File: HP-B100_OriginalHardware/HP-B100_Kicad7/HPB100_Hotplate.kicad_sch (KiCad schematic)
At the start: 62 parts, among them J1 01x03_RM3.96mm, J2 01x02_JST_RM2.54mm, J3 Conn_01x03, J4 01x04_RM8.25mm, J5 Screw_Terminal_01x02, J6 Conn_01x09, J7 Conn_01x06, J8 Conn_01x10, Q1 BTA16-800B, SW1 SW_Push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

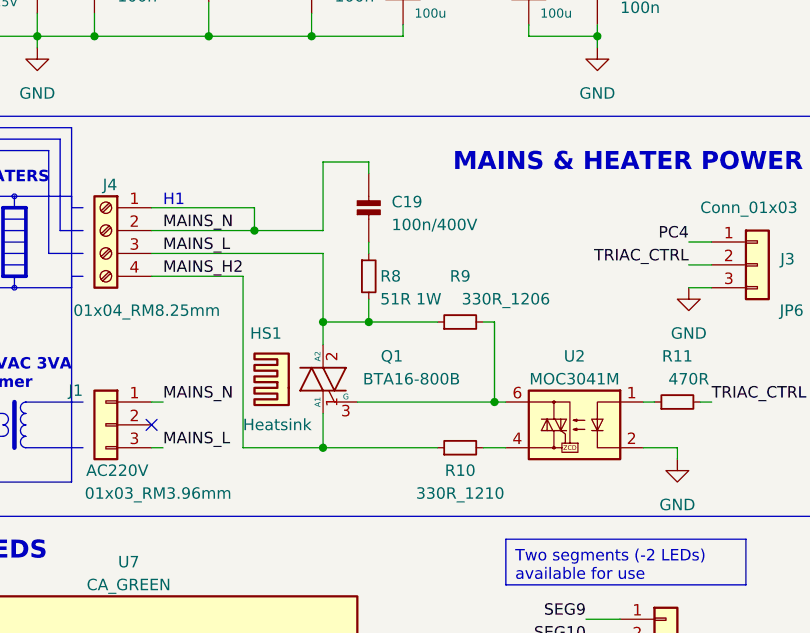
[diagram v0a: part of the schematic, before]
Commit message: fixed snubber circuit
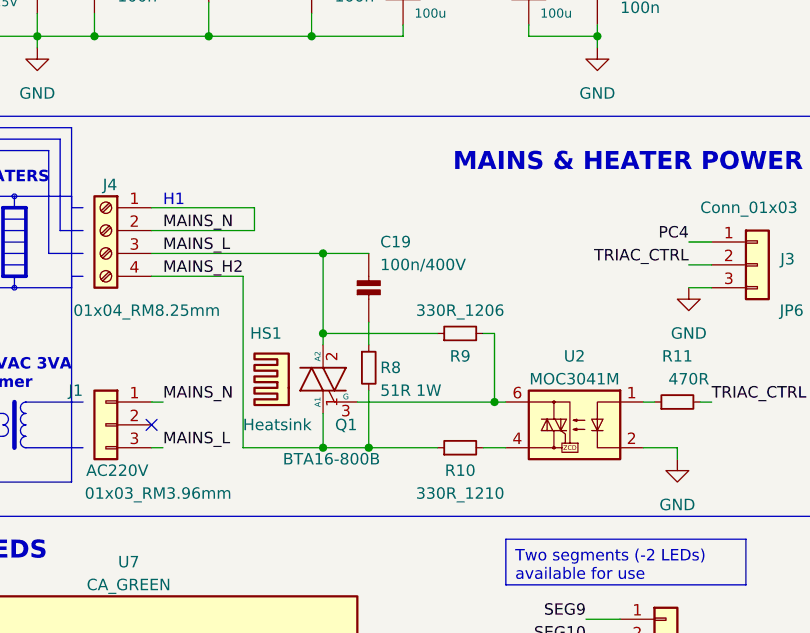
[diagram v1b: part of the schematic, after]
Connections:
- net MAINS_H2: now also R8.2
- net MAINS_L: now also C19.1; no longer R8.2
- net MAINS_N: no longer C19.1
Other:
- moved on the sheet: C19, R8, R9
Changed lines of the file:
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@@
   (junction (at 46.99 167.64) (diameter 0) (color 0 0 0 0)
   )
-  (junction (at 77.47 73.66) (diameter 0) (color 0 0 0 0)
+  (junction (at 77.47 74.93) (diameter 0) (color 0 0 0 0)
   )
   (junction (at 241.3 134.62) (diameter 0) (color 0 0 0 0)
   )
+  (junction (at 82.55 87.63) (diameter 0) (color 0 0 0 0)
+  )
   (junction (at 160.02 147.32) (diameter 0) (color 0 0 0 0)
   )
@@
   (junction (at 142.24 175.26) (diameter 0) (color 0 0 0 0)
   )
-  (junction (at 82.55 73.66) (diameter 0) (color 0 0 0 0)
-  )
   (junction (at 86.36 30.48) (diameter 0) (color 0 0 0 0)
   )
@@
   (junction (at 208.28 116.84) (diameter 0) (color 0 0 0 0)
   )
-  (junction (at 69.85 63.5) (diameter 0) (color 0 0 0 0)
-  )
   (junction (at 196.85 116.84) (diameter 0) (color 0 0 0 0)
   )
@@
   (junction (at 45.72 30.48) (diameter 0) (color 0 0 0 0)
   )
+  (junction (at 77.47 66.04) (diameter 0) (color 0 0 0 0)
+  )
   (junction (at 260.35 125.73) (diameter 0) (color 0 0 0 0)
   )
@@
     (stroke (width 0) (type default))
   )
+  (wire (pts (xy 82.55 87.63) (xy 90.17 87.63))
+    (stroke (width 0) (type default))
+  )
   (wire (pts (xy 24.13 140.97) (xy 29.21 140.97))
     (stroke (width 0) (type default))
@@
     (stroke (width 0) (type default))
   )
+  (wire (pts (xy 77.47 74.93) (xy 77.47 76.2))
+    (stroke (width 0) (type default))
+  )
   (wire (pts (xy 68.58 68.58) (xy 68.58 87.63))
     (stroke (width 0) (type default))
@@
     (stroke (width 0) (type default))
   )
-  (wire (pts (xy 82.55 64.77) (xy 82.55 66.04))
+  (wire (pts (xy 82.55 73.66) (xy 82.55 76.2))
     (stroke (width 0) (type default))
   )
@@
     (stroke (width 0) (type default))
   )
-  (wire (pts (xy 82.55 71.12) (xy 82.55 73.66))
-    (stroke (width 0) (type default))
-  )
   (wire (pts (xy 45.72 30.48) (xy 52.07 30.48))
     (stroke (width 0) (type default))
@@
     (stroke (width 0) (type default))
   )
-  (wire (pts (xy 77.47 66.04) (xy 77.47 73.66))
-    (stroke (width 0) (type default))
-  )
   (polyline (pts (xy 38.1 66.04) (xy 40.64 66.04))
     (stroke (width 0) (type default))
@@
     (stroke (width 0) (type default))
   )
-  (wire (pts (xy 82.55 73.66) (xy 77.47 73.66))
+  (wire (pts (xy 77.47 74.93) (xy 90.17 74.93))
     (stroke (width 0) (type default))
   )
@@
     (stroke (width 0) (type default))
   )
-  (wire (pts (xy 82.55 55.88) (xy 82.55 57.15))
-    (stroke (width 0) (type default))
-  )
   (wire (pts (xy 266.7 22.86) (xy 269.24 22.86))
     (stroke (width 0) (type default))
@@
     (stroke (width 0) (type default))
   )
-  (wire (pts (xy 77.47 63.5) (xy 77.47 55.88))
-    (stroke (width 0) (type default))
-  )
   (wire (pts (xy 72.39 30.48) (xy 76.2 30.48))
     (stroke (width 0) (type default))
@@
     (stroke (width 0) (type default))
   )
-  (wire (pts (xy 69.85 63.5) (xy 77.47 63.5))
-    (stroke (width 0) (type default))
-  )
   (wire (pts (xy 76.2 30.48) (xy 86.36 30.48))
     (stroke (width 0) (type default))
@@
     (stroke (width 0) (type default))
   )
-  (wire (pts (xy 82.55 73.66) (xy 90.17 73.66))
-    (stroke (width 0) (type default))
-  )
   (wire (pts (xy 154.94 134.62) (xy 160.02 134.62))
     (stroke (width 0) (type default))
@@
     (stroke (width 0) (type default))
   )
-  (wire (pts (xy 96.52 73.66) (xy 95.25 73.66))
+  (wire (pts (xy 96.52 74.93) (xy 95.25 74.93))
     (stroke (width 0) (type default))
   )
@@
     (stroke (width 0) (type default))
   )
-  (wire (pts (xy 77.47 87.63) (xy 90.17 87.63))
+  (wire (pts (xy 77.47 87.63) (xy 82.55 87.63))
     (stroke (width 0) (type default))
   )
@@
     (stroke (width 0) (type default))
   )
-  (wire (pts (xy 77.47 55.88) (xy 82.55 55.88))
-    (stroke (width 0) (type default))
-  )
   (wire (pts (xy 106.68 109.22) (xy 110.49 109.22))
     (stroke (width 0) (type default))
@@
     (stroke (width 0) (type default))
   )
+  (wire (pts (xy 82.55 81.28) (xy 82.55 87.63))
+    (stroke (width 0) (type default))
+  )
   (polyline (pts (xy 283.21 48.26) (xy 283.21 13.97))
     (stroke (width 0) (type default))
@@
     (stroke (width 0) (type default))
   )
+  (wire (pts (xy 77.47 66.04) (xy 77.47 74.93))
+    (stroke (width 0) (type default))
+  )
   (wire (pts (xy 265.43 72.39) (xy 269.24 72.39))
     (stroke (width 0) (type default))
@@
     (stroke (width 0) (type default))
   )
+  (wire (pts (xy 82.55 66.04) (xy 77.47 66.04))
+    (stroke (width 0) (type default))
+  )
   (wire (pts (xy 149.86 157.48) (xy 147.32 157.48))
     (stroke (width 0) (type default))
@@
     (stroke (width 0) (type default))
   )
-  (wire (pts (xy 96.52 82.55) (xy 96.52 73.66))
+  (wire (pts (xy 96.52 82.55) (xy 96.52 74.93))
     (stroke (width 0) (type default))
   )
@@
     (stroke (width 0) (type default))
   )
-  (wire (pts (xy 77.47 73.66) (xy 77.47 76.2))
-    (stroke (width 0) (type default))
-  )
   (polyline (pts (xy 41.91 64.77) (xy 44.45 64.77))
     (stroke (width 0) (type default))
@@
     )
   )
-  (symbol (lib_id "H_passives:CAP_NP") (at 82.55 60.96 0) (unit 1)
-    (in_bom yes) (on_board yes) (dnp no) (fields_autoplaced)
-    (property "Reference" "C19" (at 85.09 60.325 0)
+  (symbol (lib_id "H_passives:CAP_NP") (at 82.55 69.85 0) (unit 1)
+    (in_bom yes) (on_board yes) (dnp no)
+    (property "Reference" "C19" (at 83.82 64.77 0)
       (effects (font (size 1.27 1.27)) (justify left))
     )
-    (property "Value" "100n/400V" (at 85.09 62.865 0)
+    (property "Value" "100n/400V" (at 83.82 67.31 0)
       (effects (font (size 1.27 1.27)) (justify left))
     )
-    (property "Footprint" "" (at 82.55 62.23 0)
+    (property "Footprint" "" (at 82.55 71.12 0)
       (effects (font (size 1.27 1.27)) hide)
     )
-    (property "Datasheet" "" (at 82.55 62.23 0)
+    (property "Datasheet" "" (at 82.55 71.12 0)
       (effects (font (size 1.27 1.27)) hide)
     )
@@
     )
   )
-  (symbol (lib_id "Device:R_Small") (at 92.71 73.66 90) (unit 1)
+  (symbol (lib_id "Device:R_Small") (at 92.71 74.93 90) (unit 1)
     (in_bom yes) (on_board yes) (dnp no)
-    (property "Reference" "R9" (at 92.71 68.58 90)
+    (property "Reference" "R9" (at 92.71 77.47 90)
       (effects (font (size 1.27 1.27)))
     )
-    (property "Value" "330R_1206" (at 97.79 71.12 90)
+    (property "Value" "330R_1206" (at 92.71 72.39 90)
       (effects (font (size 1.27 1.27)))
     )
-    (property "Footprint" "" (at 92.71 73.66 0)
+    (property "Footprint" "" (at 92.71 74.93 0)
       (effects (font (size 1.27 1.27)) hide)
     )
-    (property "Datasheet" "~" (at 92.71 73.66 0)
+    (property "Datasheet" "~" (at 92.71 74.93 0)
       (effects (font (size 1.27 1.27)) hide)
     )
@@
   (symbol (lib_id "Triac_Thyristor:BTA16-800B") (at 77.47 80.01 0) (mirror y) (unit 1)
     (in_bom yes) (on_board yes) (dnp no)
-    (property "Reference" "Q1" (at 86.36 77.47 0)
+    (property "Reference" "Q1" (at 81.28 85.09 0)
       (effects (font (size 1.27 1.27)) (justify left))
     )
-    (property "Value" "BTA16-800B" (at 92.71 80.01 0)
+    (property "Value" "BTA16-800B" (at 83.82 88.9 0)
       (effects (font (size 1.27 1.27)) (justify left))
     )
@@
     )
   )
-  (symbol (lib_id "Device:R_Small") (at 82.55 68.58 0) (unit 1)
+  (symbol (lib_id "Device:R_Small") (at 82.55 78.74 0) (unit 1)
     (in_bom yes) (on_board yes) (dnp no)
-    (property "Reference" "R8" (at 83.82 68.58 0)
+    (property "Reference" "R8" (at 83.82 78.74 0)
       (effects (font (size 1.27 1.27)) (justify left))
     )
-    (property "Value" "51R 1W" (at 83.82 71.12 0)
+    (property "Value" "51R 1W" (at 83.82 81.28 0)
       (effects (font (size 1.27 1.27)) (justify left))
     )
-    (property "Footprint" "" (at 82.55 68.58 0)
+    (property "Footprint" "" (at 82.55 78.74 0)
       (effects (font (size 1.27 1.27)) hide)
     )
-    (property "Datasheet" "~" (at 82.55 68.58 0)
+    (property "Datasheet" "~" (at 82.55 78.74 0)
       (effects (font (size 1.27 1.27)) hide)
     )
